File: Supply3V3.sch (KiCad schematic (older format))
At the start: 32 parts, among them Q4 BSS138, Q7 CSD18503Q5A, U7 LM25088-1MH

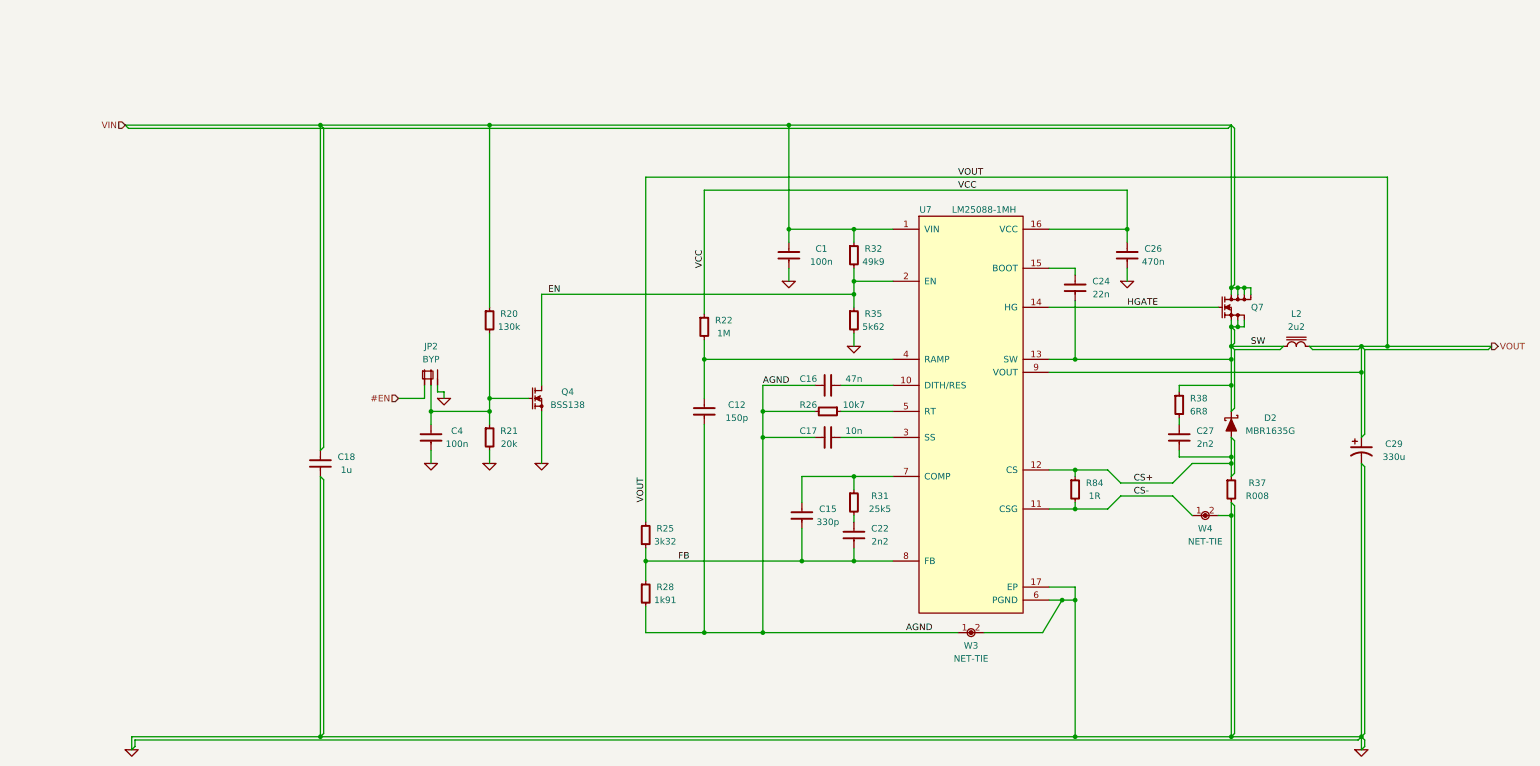
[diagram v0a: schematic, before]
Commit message: Reannotated parts
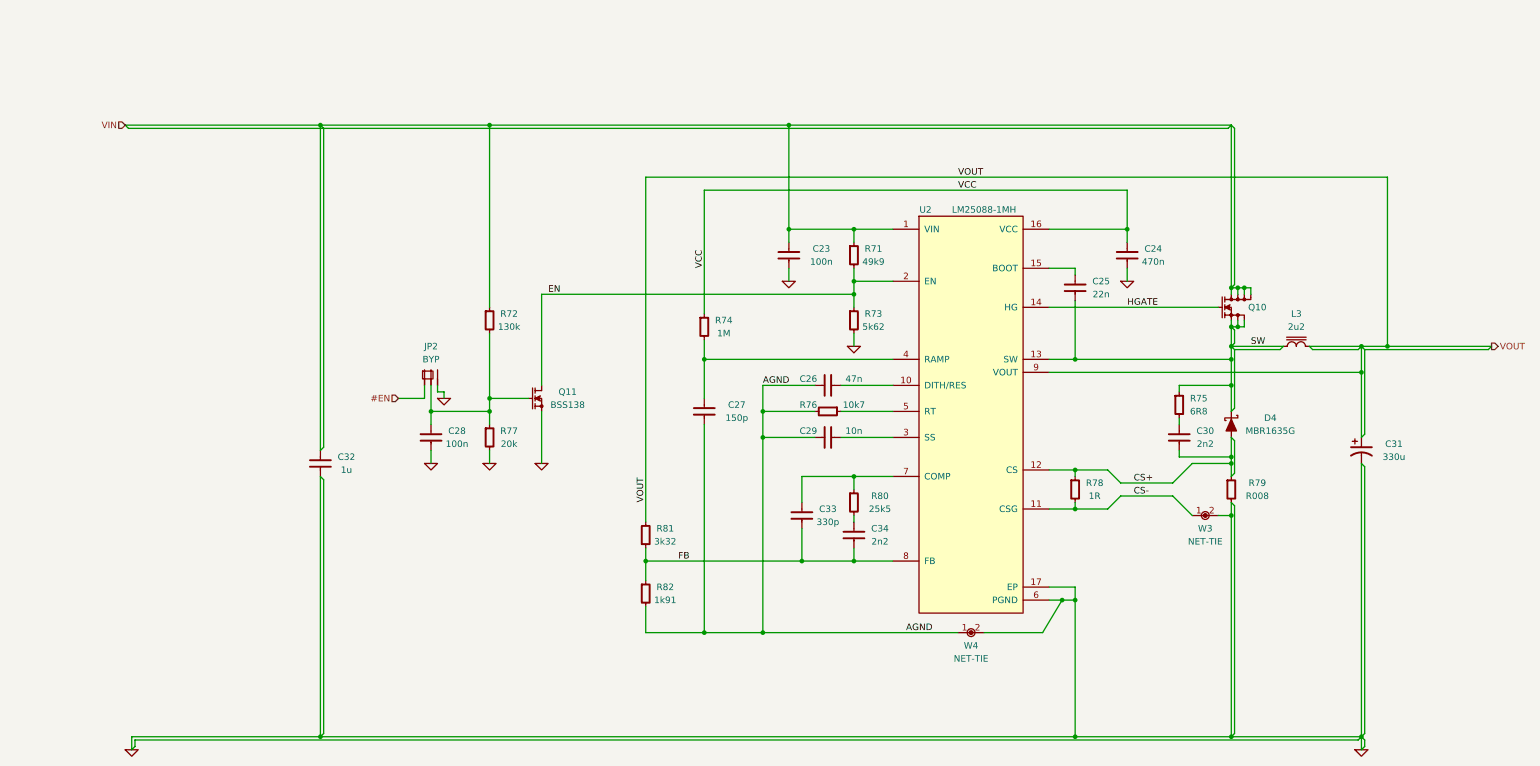
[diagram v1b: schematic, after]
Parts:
- renumbered C1 to C23, C26 to C24, C24 to C25, C16 to C26, C12 to C27, C4 to C28, C17 to C29, C27 to C30, C29 to C31, C18 to C32, C15 to C33, C22 to C34, D2 to D4, L2 to L3, Q7 to Q10, Q4 to Q11, R32 to R71, R20 to R72, R35 to R73, R22 to R74, R38 to R75, R26 to R76, R21 to R77, R84 to R78, R37 to R79, R31 to R80, R25 to R81, R28 to R82, U7 to U2, W4 to W3, W3 to W4

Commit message: Silkscreen and 3D touchups
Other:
- moved on the sheet: C23, C24, C25, C26, C27, C28, C29, C30, C31, C32, C33, C34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

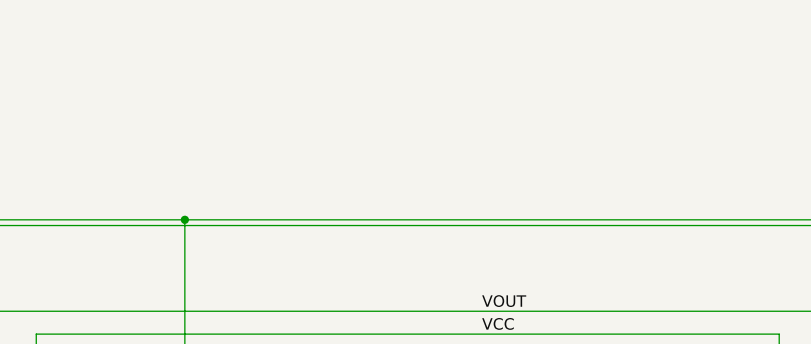
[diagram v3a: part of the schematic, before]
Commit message: Researched alternative DC-DC controllers
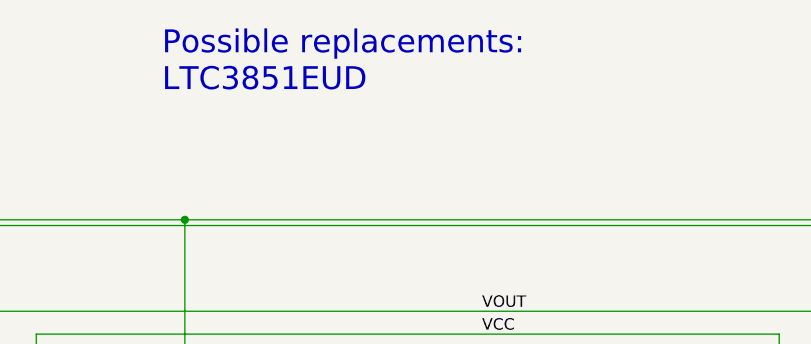
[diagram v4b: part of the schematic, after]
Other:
- note added: "Possible replacements:\nLTC3851EUD"
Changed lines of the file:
@@
 	3000 2800 3000 3500
 Connection ~ 5400 2800
+Text Notes 4800 950  0    100  ~ 0
+Possible replacements:\nLTC3851EUD
 $EndSCHEMATC

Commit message: Changed BSS138 to MMUN221
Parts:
- removed Q11: BSS138, smd-semi:SOT-23, symbol BSS138
- removed R77: 20k, IPC7351-Nominal:RESC1005X40, symbol R-0402
- added Q11: MMUN2231L, smd-semi:SOT-23, symbol MMUN2231L
- R72: value 130k -> 22k
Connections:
- net EN: now also Q11.3
- net GND: now also Q11.2
- net at C28.1, JP2.2, R72.2: now also Q11.1
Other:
- note removed: "Possible replacements:\nLTC3851EUD"
- moved on the sheet: C28
